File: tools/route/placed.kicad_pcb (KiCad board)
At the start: 2 copper layers, 150 x 95 mm, 159 parts, among them J1 USB-C 16P, J110 MAINS IN L/N, J111 K1 L/COM/NO, J112 K2 L/COM/NO, J113 K3 L/COM/NO, J114 K4 L/COM/NO, J115 END SW 1/2/3, J116 DEMAND 230V/24V/RET, J201 OT (24V max), J3 FLOW, J4 OUTDOOR, J5 OLED, J6 QWIIC, J7 SPARE, J8 BOOT_JP, K101 HF32FA-G/005-HSL1, K102 HF32FA-G/005-HSL1, K103 HF32FA-G/005-HSL1, K104 HF32FA-G/005-HSL1 (DNP), Q101 AO3400A, Q102 AO3400A, Q103 AO3400A, Q104 AO3400A, Q201 S8550, SW1 RESET, SW2 BOOT, SW3 BTN1, SW4 BTN2, U1 ESP32-C6-WROOM-1-N8, U101 LTV-817S, U102 LTV-817S, U103 LTV-817S, U104 LTV-817S, U105 LTV-817S, U2 AMS1117-3.3, U201 LTV-817S (TX), U202 LTV-817S (RX), U3 USBLC6-2SC6

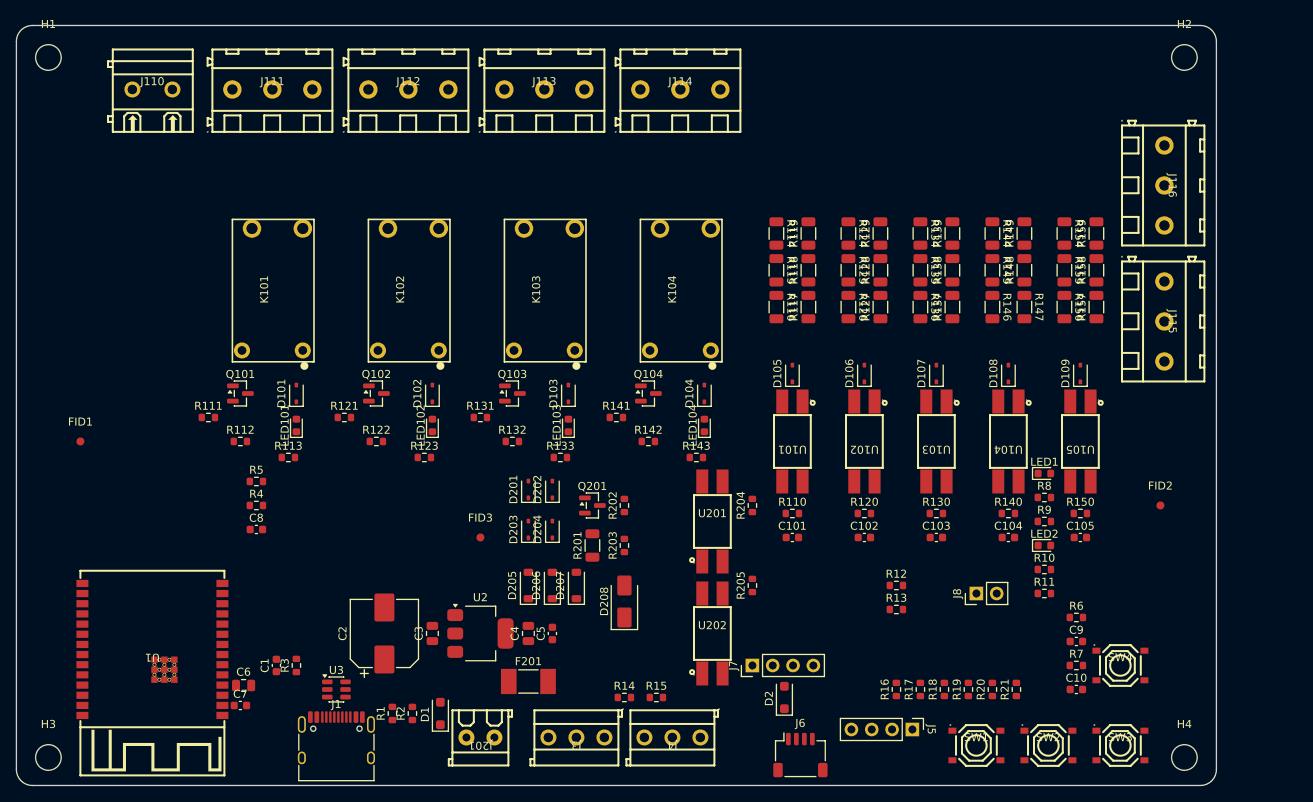
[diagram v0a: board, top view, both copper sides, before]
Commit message: Andiron v1.0 redesign: volt-free changeover relays, no mains sensing, layout by module area
- Relays: four HF115F/005-1ZS3A changeover relays (CH1-CH4), each with its own
  NC/COM/NO terminal, as UK heating controllers present their outputs; 5 kV
  VDE-reinforced coil-to-contact insulation. Each channel is its own net class
  and keeps 6.4 mm clearance and creepage from everything that is not itself.
- Removed the 230 V supply input, L/N rails and all five mains sensing inputs
  (30 resistors, 5 optos, end-switch and demand terminals). The only mains on
  the board is the relay contacts.
- Power: LDL1117S33R replaces the AMS1117 (0.35 V dropout, ceramic-stable,
  18 V abs-max, no heat-spreading copper); relays run from USB 5 V directly.
- OLED header fixed to GND/3V3/SCL/SDA (option resistors removed); freed GPIOs
  on an 8-pin spare header; Mains IO sheet renamed Relays.
- Layout regenerated by module area (relay strip, drivers, MCU with antenna at
  the left edge, power, OpenTherm, sensors, controls), 150 x 90 mm. Placement
  and shared geometry now in tools/layout/; tools/sync_netlist.py syncs the
  schematic to the board headlessly.
- Low-voltage clearance 0.25 mm so module pins escape straight out; USB nets
  get their own 0.2 mm class. Pipeline widens router neck-down stubs; stitching
  and island-repair vias avoid pads.
- Silkscreen relabelled in plain language (CH1 NC COM NO, OPENTHERM, FLOW TEMP,
  OUTDOOR TEMP, ...); repository URL removed.
- Docs: requirements and design brief rewritten for v1.0, schematic plan,
  README, BOM, renders, schematic PDF and layout lessons updated.

ERC 0 errors; DRC 0 errors, 0 unconnected, parity clean; sanity PASS.
BOM: ~$15.77 -> ~$24.03 components per board (~$28.97 -> ~$37.23 at 5 incl.
fees), mostly the four HF115F relays.

Co-Authored-By: Claude Opus 5.5 <noreply@anthropic.com>
Claude-Session: https://claude.ai/code/session_01XDSh2Z4phxf7z2Gu1153CL
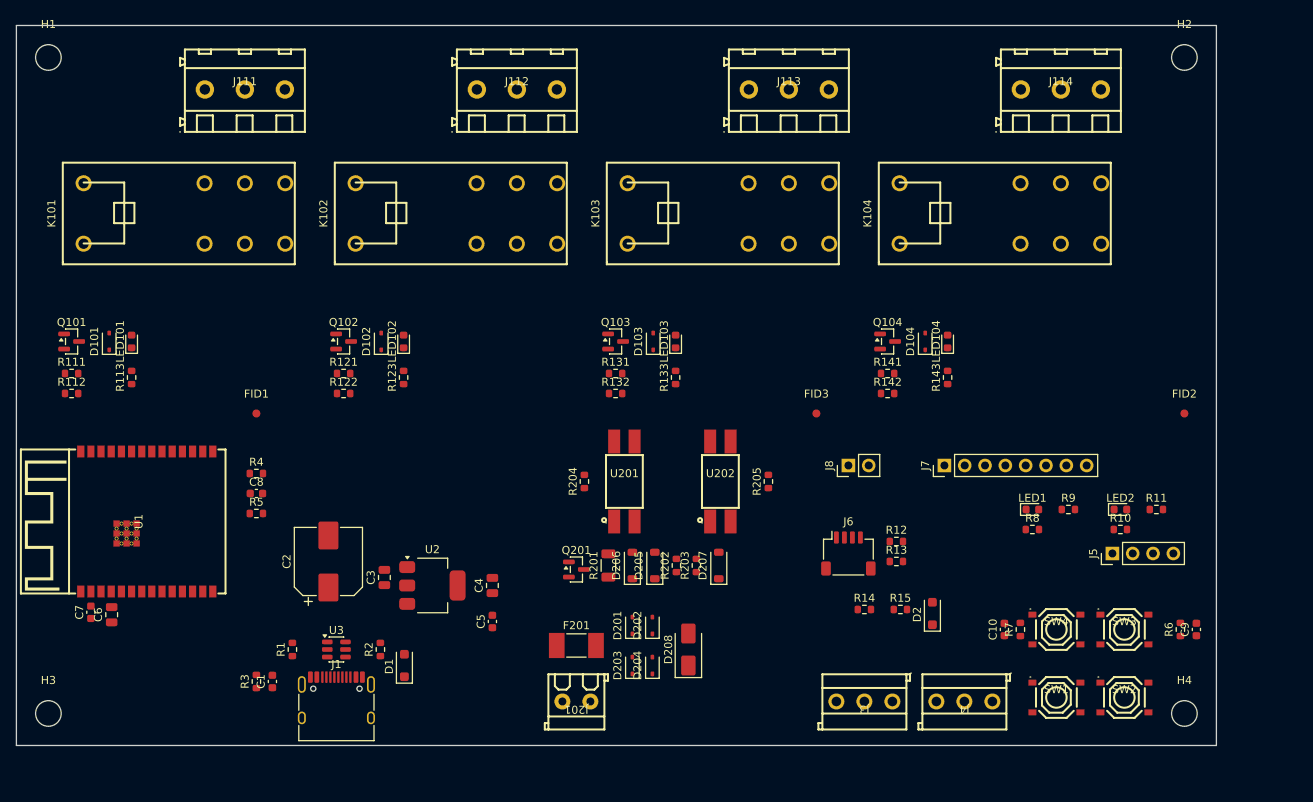
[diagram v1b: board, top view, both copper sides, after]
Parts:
- removed C101, C102, C103, C104, C105: 1uF, Capacitor_SMD:C_0603_1608Metric
- removed D105, D106, D107, D108, D109: 1N4148WS, Diode_SMD:D_SOD-323
- removed J110: MAINS IN L/N, jlc:CONN-TH_2P-P5.00_WJ128V-5.0-2P
- removed J115: END SW 1/2/3, jlc:CONN-TH_3P-P5.00_WJ128V-5.0-3P
- removed J116: DEMAND 230V/24V/RET, jlc:CONN-TH_3P-P5.00_WJ128V-5.0-3P
- removed R110, R120, R130, R140, R150: 220k, Resistor_SMD:R_0603_1608Metric
- removed R114, R115, R116, R117, R118, R119, R124, R125, R126, R127, R128, R129, R134, R135, R136, R137, R138, R139, R144, R145, R146, R147, R148, R149, R154, R155, R156, R157, R158, R159: 22k, Resistor_SMD:R_1206_3216Metric
- removed R16, R18, R20: 0R, Resistor_SMD:R_0603_1608Metric
- removed R17, R19, R21: 0R (DNP), Resistor_SMD:R_0603_1608Metric
- removed U101, U102, U103, U104, U105: LTV-817S, jlc:OPTO-SMD-4_L4.6-W6.5-P2.54-LS10.3-BL
- J5: value OLED -> OLED GND/3V3/SCL/SDA
- J7: value SPARE -> SPARE GPIO; footprint Connector_PinHeader_2.54mm:PinHeader_1x04_P2.54mm_Vertical -> Connector_PinHeader_2.54mm:PinHeader_1x08_P2.54mm_Vertical
- K101, K102, K103: value HF32FA-G/005-HSL1 -> HF115F/005-1ZS3A; footprint jlc:RELAY-TH_HF32FA-XX-HXX1X -> jlc:RELAY-TH_HF115F-024-2ZS4
- K104: value HF32FA-G/005-HSL1 (DNP) -> HF115F/005-1ZS3A; footprint jlc:RELAY-TH_HF32FA-XX-HXX1X -> jlc:RELAY-TH_HF115F-024-2ZS4
- U2: value AMS1117-3.3 -> LDL1117S33R
- moved J114 47.6 mm to (130.6, 8.00)
- moved FID3 44.8 mm to (100.0, 48.5)
- moved K104 41.1 mm to (123.0, 23.5)
- moved J4 36.8 mm to (118.5, 84.5)
- moved J3 36.3 mm to (106.0, 84.5)
- moved J7 34.7 mm to (116.0, 55.0)
- moved R141 34.3 mm to (108.9, 43.5)
- moved J5 33.3 mm to (137.0, 66.0), turned to 90 degrees
- moved R143 33.0 mm to (116.4, 44.0), turned to 90 degrees
- moved R15 32.4 mm to (110.5, 73.0)
- moved LED104 32.2 mm to (116.4, 39.5)
- moved R14 32.0 mm to (106.0, 73.0)
- moved Q104 30.6 mm to (108.9, 39.5)
- moved J113 30.6 mm to (96.6, 8.00)
- moved R142 30.5 mm to (108.9, 46.0)
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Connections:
- net /Mains IO/COIL1 renamed /Relays/COIL1
- net /Mains IO/COIL2 renamed /Relays/COIL2
- net /Mains IO/COIL3 renamed /Relays/COIL3
- net /Mains IO/COIL4 renamed /Relays/COIL4
- net /Mains IO/G1 renamed /Relays/G1
- net /Mains IO/G2 renamed /Relays/G2
- net /Mains IO/G3 renamed /Relays/G3
- net /Mains IO/G4 renamed /Relays/G4
- net /Mains IO/LEDR1 renamed /Relays/LEDR1
- net /Mains IO/LEDR2 renamed /Relays/LEDR2
- net /Mains IO/LEDR3 renamed /Relays/LEDR3
- net /Mains IO/LEDR4 renamed /Relays/LEDR4
- J111 pad 1: /Mains IO/MAINS_L -> /Relays/NC1
- J111 pad 2: /Mains IO/COM1 -> /Relays/COM1
- J111 pad 3: /Mains IO/NO1 -> /Relays/NO1
- J112 pad 1: /Mains IO/MAINS_L -> /Relays/NC2
- J112 pad 2: /Mains IO/COM2 -> /Relays/COM2
- J112 pad 3: /Mains IO/NO2 -> /Relays/NO2
- J113 pad 1: /Mains IO/MAINS_L -> /Relays/NC3
- J113 pad 2: /Mains IO/COM3 -> /Relays/COM3
- J113 pad 3: /Mains IO/NO3 -> /Relays/NO3
- J114 pad 1: /Mains IO/MAINS_L -> /Relays/NC4
- J114 pad 2: /Mains IO/COM4 -> /Relays/COM4
- J114 pad 3: /Mains IO/NO4 -> /Relays/NO4
- J5 pad 1: /Power + MCU/OLED_P1 -> GND
- J5 pad 2: /Power + MCU/OLED_P2 -> +3V3
- J7 pad 3: +3V3 -> /Power + MCU/IO10
- J7 pad 4: GND -> /Power + MCU/IO11
- K101 pad 3: /Mains IO/COM1 -> /Relays/NC1
- K101 pad 4: /Mains IO/NO1 -> /Relays/NC1
- K102 pad 3: /Mains IO/COM2 -> /Relays/NC2
- K102 pad 4: /Mains IO/NO2 -> /Relays/NC2
- K103 pad 3: /Mains IO/COM3 -> /Relays/NC3
- K103 pad 4: /Mains IO/NO3 -> /Relays/NC3
- K104 pad 3: /Mains IO/COM4 -> /Relays/NC4
- K104 pad 4: /Mains IO/NO4 -> /Relays/NC4
- U1 pad 11: /ES1 -> /Power + MCU/IO10
- U1 pad 12: /ES2 -> /Power + MCU/IO11
- U1 pad 16: /ES3 -> /Power + MCU/IO18
- U1 pad 17: /DEMAND_IN -> /Power + MCU/IO19
- U1 pad 18: /MAINS_OK -> unconnected-(U1-IO20-Pad18)
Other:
- board size 150 x 95 mm -> 150 x 90 mm

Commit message: Wall-hanging layout, cheaper parts, OLED area
Layout (160 x 95 mm): the board hangs on a wall with every cable from below
or the left. Relay and OpenTherm terminals on the bottom edge, USB-C, FLOW,
OUTDOOR and Qwiic on the left edge, antenna at the top edge. The OLED module
stacks in landscape over a reserved top-right area.

Parts: TE RT314005 relays replace the HF115F (same body and pin grid,
reinforced 5 kV / 10 mm insulation, flux-proof so no washing after THT); AEM
MF2410F1.000TM fast fuse replaces the Bourns (same breaking capacity and
I2t, Bourns nearly out of stock); Basic 100 nF and 1 uF capacitors.
Per-board total at 5: $37.23 -> $27.86 (components $24.03 -> $15.86).

Tooling: locked +5V rail and supply feed (Freerouting would not route the
net), USB-C pre-routes drawn in the receptacle's own frame, router keep-outs
over the isolation slots, temporary zones stripped in a text pass, wider
pour-island repair, a pre-routing placement check, and sanity checks for
connector edges, no-cable edges and the OLED area.

Co-Authored-By: Claude Opus 5.5 <noreply@anthropic.com>
Claude-Session: https://claude.ai/code/session_01XDSh2Z4phxf7z2Gu1153CL
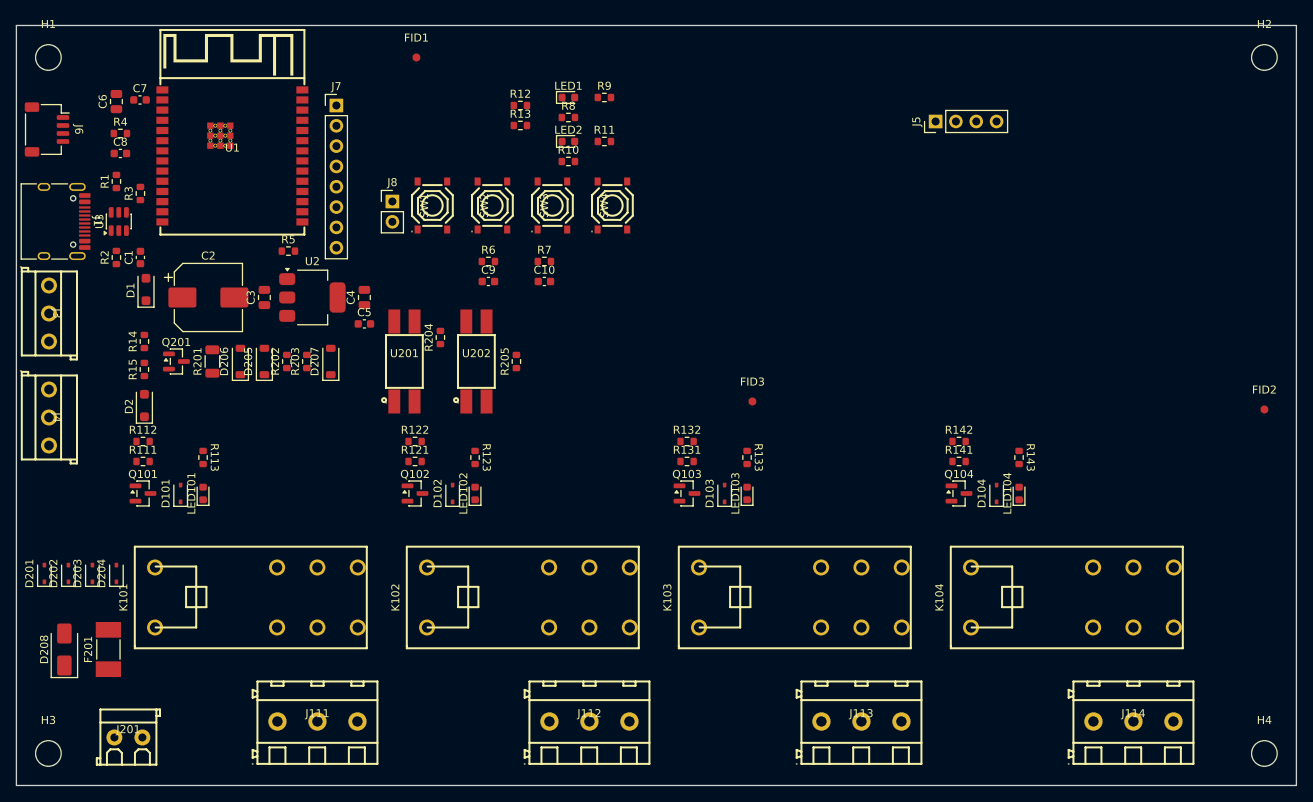
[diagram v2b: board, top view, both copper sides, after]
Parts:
- J111: value K1 L/COM/NO -> CH1 NC/COM/NO
- J112: value K2 L/COM/NO -> CH2 NC/COM/NO
- J113: value K3 L/COM/NO -> CH3 NC/COM/NO
- J114: value K4 L/COM/NO -> CH4 NC/COM/NO
- K101, K102, K103, K104: value HF115F/005-1ZS3A -> RT314005; footprint jlc:RELAY-TH_HF115F-024-2ZS4 -> jlc:RELAY-TH_RT314005_HF115F-PINS
- moved J4 119.8 mm to (4.08, 49.0), turned to -90 degrees
- moved J6 113.3 mm to (3.83, 13.0), turned to -90 degrees
- moved J3 112.9 mm to (4.08, 36.0), turned to -90 degrees
- moved D2 101.9 mm to (16.0, 47.5)
- moved SW2 100.1 mm to (59.5, 22.5), turned to 90 degrees
- moved SW1 99.3 mm to (52.0, 22.5), turned to 90 degrees
- moved R15 99.1 mm to (16.0, 43.0), turned to 90 degrees
- moved C9 98.6 mm to (59.0, 32.0), turned to 0 degrees
- moved R6 98.0 mm to (59.0, 29.5), turned to 0 degrees
- moved R14 96.0 mm to (16.0, 39.5), turned to 90 degrees
- moved SW3 89.0 mm to (67.0, 22.5), turned to 90 degrees
- moved J7 88.3 mm to (40.0, 10.0), turned to 0 degrees
- moved LED2 82.9 mm to (69.0, 14.5)
- moved R10 82.9 mm to (69.0, 17.0)
- moved R11 82.9 mm to (73.5, 14.5)
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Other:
- board size 150 x 90 mm -> 160 x 95 mm

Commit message: OLED on a Qwiic cable, boot jumper removed, enclosure re-sized
- J5 (OLED) is a Qwiic socket, same part as J6, in Qwiic order GND / 3V3 /
  SDA / SCL on GPIO6/GPIO7 (hardware I2C). The module sits in the cover
  window on a short cable (JST-SH to Dupont, or a soldered pigtail); the
  2.9 mm socket replaces a header that needed ~20 mm with Dupont housings.
- J8 (boot jumper) removed from schematic and board: the BOOT button does
  the same.
- Enclosure section rewritten: ~170 x 135 x 32 mm with a mains wiring bay
  (cable clamps, OT/mains rib), standoffs and support posts, USB-C wall
  relief, lid plungers for BTN1/BTN2.
- route_board.py no longer drops a stitching via that a GND track ends on
  (it disconnected a route after this re-route).
- Board re-routed; ERC/DRC/parity/sanity clean. 15 -> 13 Extended parts;
  estimate at 5 boards incl. fees $24.79 -> $23.76 per board.

Co-Authored-By: Claude Opus 5.5 <noreply@anthropic.com>
Claude-Session: https://claude.ai/code/session_01XDSh2Z4phxf7z2Gu1153CL
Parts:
- removed J8: BOOT_JP, Connector_PinHeader_2.54mm:PinHeader_1x02_P2.54mm_Vertical
- J5: value OLED GND/3V3/SCL/SDA -> OLED (Qwiic) GND/3V3/SDA/SCL; footprint Connector_PinHeader_2.54mm:PinHeader_1x04_P2.54mm_Vertical -> Connector_JST:JST_SH_SM04B-SRSS-TB_1x04-1MP_P1.00mm_Horizontal
- moved J5 3.83 mm to (118.7, 11.5), turned to 0 degrees
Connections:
- J5 pad 3: /Power + MCU/SCL -> /Power + MCU/SDA
- J5 pad 4: /Power + MCU/SDA -> /Power + MCU/SCL
